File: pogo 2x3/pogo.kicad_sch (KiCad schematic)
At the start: 2 parts, among them J1 AVR-ISP-6, J2 PinHeader_1x06_P2.54mm_Horizo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

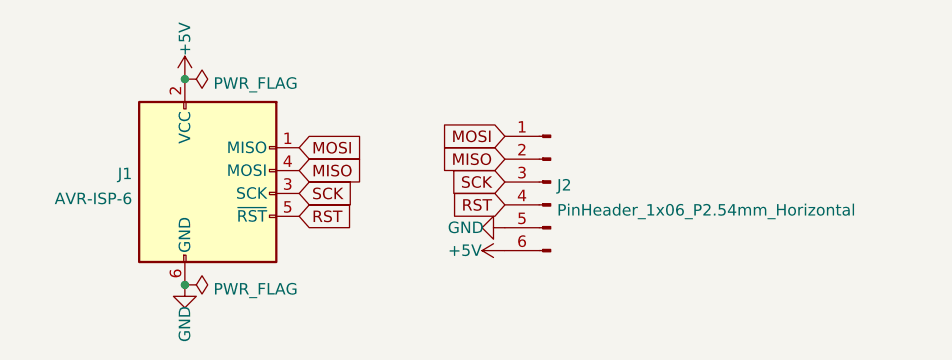
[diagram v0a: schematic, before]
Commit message: fixed pogo and dip adapter
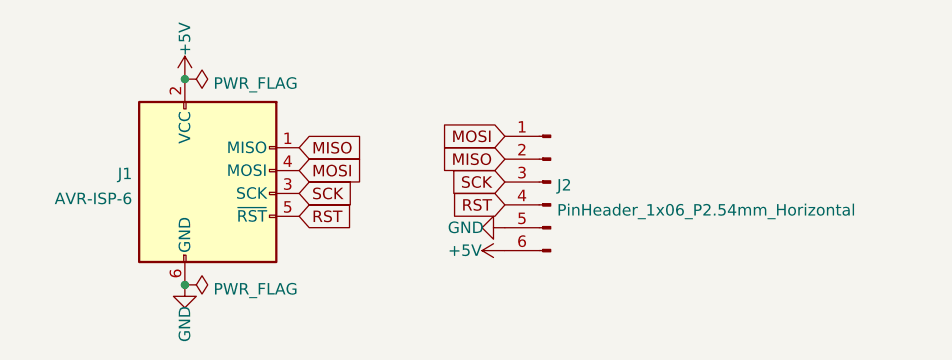
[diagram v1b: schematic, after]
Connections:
- net MISO: now also J1.1 (MISO); no longer J1.4 (MOSI)
- net MOSI: now also J1.4 (MOSI); no longer J1.1 (MISO)
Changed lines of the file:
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@@
     )
   )
-  (global_label "MOSI" (shape input) (at 169.545 89.535 0) (fields_autoplaced)
+  (global_label "MOSI" (shape input) (at 169.545 92.075 0) (fields_autoplaced)
     (effects (font (size 1.27 1.27)) (justify left))
-    (property "Intersheet References" "${INTERSHEET_REFS}" (id 0) (at 176.7448 89.4556 0)
+    (property "Intersheet References" "${INTERSHEET_REFS}" (id 0) (at 176.7448 91.9956 0)
       (effects (font (size 1.27 1.27)) (justify left) hide)
     )
@@
     )
   )
-  (global_label "MISO" (shape input) (at 169.545 92.075 0) (fields_autoplaced)
+  (global_label "MISO" (shape input) (at 169.545 89.535 0) (fields_autoplaced)
     (effects (font (size 1.27 1.27)) (justify left))
-    (property "Intersheet References" "${INTERSHEET_REFS}" (id 0) (at 176.7448 91.9956 0)
+    (property "Intersheet References" "${INTERSHEET_REFS}" (id 0) (at 176.7448 89.4556 0)
       (effects (font (size 1.27 1.27)) (justify left) hide)
     )
